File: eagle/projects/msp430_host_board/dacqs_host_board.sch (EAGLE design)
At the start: 91 parts, among them J1 MOL-KK-4P-V, J10 MOL-KK-3P-V, J13 JST-PH-2TH-RA, J14 USB_MICROB_RECPT, J16 MOL-KK-2-RA, J17 CLM-112-02-L-D, J18 MOL-KK-2-V, J2 MOL-KK-4P-V, J3 MOL-KK-4P-V, J4 MOL-KK-4P-V, J5 MOL-KK-5P-V, J6 MOL-KK-3P-V, J7 MOL-KK-5P-V, J8 MOL-KK-3P-RA, J9 MOL-KK-3P-V, U1 Value, U2 Value, U3 PCT2075D,118, U4 MS560702BA03-50, U5 TPS61240DRVR, U6 LP5907_DBV_5, U7 MCP73831T, U8 INA219AIDCNR, U9 STD12NF06LT4, Y1 32.768kHz, Y2 4MHz, Y3 32.768kHz, Y4 4MHz

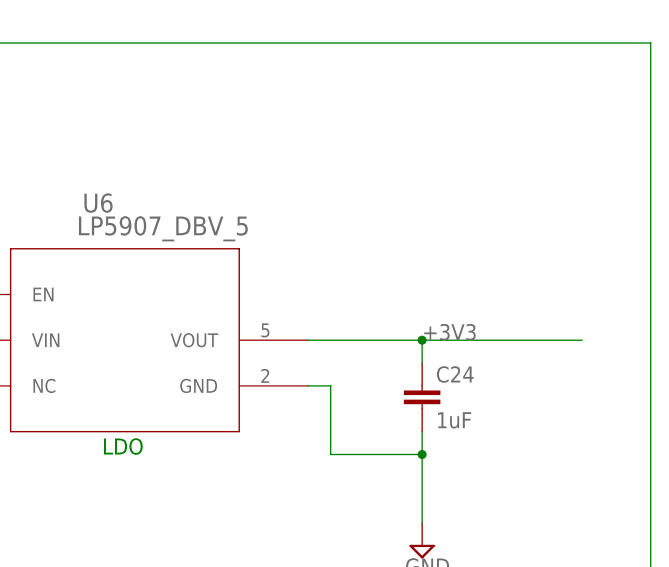
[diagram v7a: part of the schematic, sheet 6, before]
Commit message: added molex SL connectors to daqcs_host library
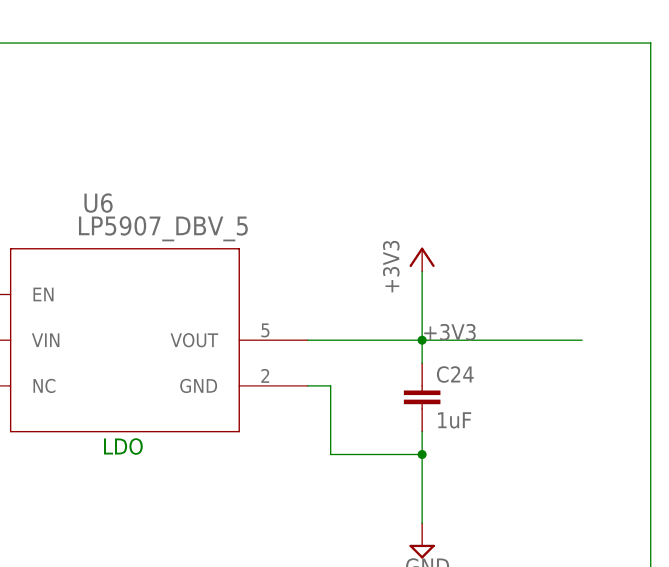
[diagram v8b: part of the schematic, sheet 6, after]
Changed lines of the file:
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@@
 <part name="J17" library="daqcs_host" deviceset="CLM-112-02-L-D" device=""/>
 <part name="J11" library="daqcs_host" deviceset="M02" device="PTH"/>
+<part name="+3V14" library="supply1" deviceset="+3V3" device=""/>
 </parts>
 <sheets>
@@
 </instance>
 <instance part="J15" gate="G$1" x="86.36" y="198.12" rot="R270"/>
+<instance part="+3V14" gate="G$1" x="327.66" y="193.04"/>
 </instances>
 <busses>
@@
 <junction x="327.66" y="182.88"/>
 <label x="327.66" y="182.88" size="1.778" layer="95"/>
-</segment>
-<segment>
+<pinref part="+3V14" gate="G$1" pin="+3V3"/>
+<wire x1="327.66" y1="182.88" x2="327.66" y2="190.5" width="0.1524" layer="91"/>
+</segment>
+<segment>
